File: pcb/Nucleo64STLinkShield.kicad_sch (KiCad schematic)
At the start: 0 parts

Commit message: Imported debug connector from design block.
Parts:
- added J1: Debug, pcb:Molex_PicoBlade_53047-1010_1x10_P1.25mm_Vertical, symbol Connector_Generic:Conn_02x05_Odd_Even
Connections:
- new net +3.3V: J1.1 (Pin_1)
- new net GND: J1.10 (Pin_10), J1.2 (Pin_2), J1.9 (Pin_9)
- new net RESET: J1.3 (Pin_3)
- new net STLINK_RX: J1.7 (Pin_7)
- new net STLINK_TX: J1.5 (Pin_5)
- new net SWCLK: J1.4 (Pin_4)
- new net SWDIO: J1.6 (Pin_6)
- new net SWO: J1.8 (Pin_8)
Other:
- note added: "Debug Connector."

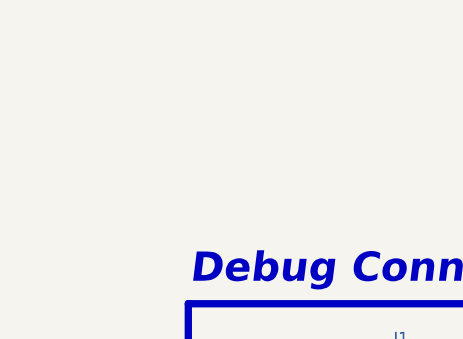
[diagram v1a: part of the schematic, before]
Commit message: Imported Nucleo-64 ST-Link debugger model.
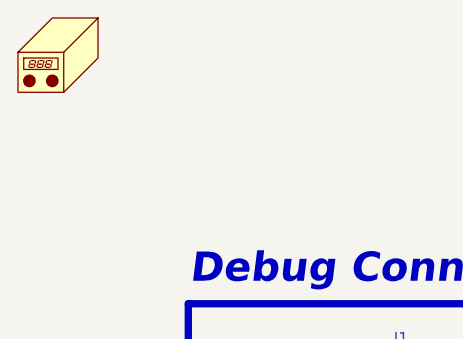
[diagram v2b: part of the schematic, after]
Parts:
- added N1: Housing, pcb:Nucleo64STLinkShieldHousing, symbol Mechanical:Housing
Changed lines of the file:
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@@
 		(dnp no)
 		(fields_autoplaced yes)
-		(property "Reference" "#PWR"
+		(property "Reference" "#PWR0101"
 			(at 142.24 100.33 0)
 			(effects
@@
 				(path "/0a179c33-cb18-4019-99e7-0e00d41f97d6/4084990c-2f2a-49e6-b0d0-e7eb5cede66f"
 					(reference "#PWR018")
+					(unit 1)
+				)
+			)
+			(project "Nucleo64STLinkShield"
+				(path "/dc931235-6a3d-461b-9fb0-f5879d72cf99"
+					(reference "#PWR0101")
+					(unit 1)
+				)
+			)
+		)
+	)
+	(symbol
+		(lib_id "Mechanical:Housing")
+		(at 107.95 62.23 0)
+		(unit 1)
+		(exclude_from_sim no)
+		(in_bom yes)
+		(on_board yes)
+		(dnp no)
+		(fields_autoplaced yes)
+		(property "Reference" "N1"
+			(at 111.76 61.2774 0)
+			(effects
+				(font
+					(size 1.27 1.27)
+				)
+				(justify left)
+				(hide yes)
+			)
+		)
+		(property "Value" "Housing"
+			(at 111.76 63.8174 0)
+			(effects
+				(font
+					(size 1.27 1.27)
+				)
+				(justify left)
+				(hide yes)
+			)
+		)
+		(property "Footprint" "pcb:Nucleo64STLinkShieldHousing"
+			(at 109.22 60.96 0)
+			(effects
+				(font
+					(size 1.27 1.27)
+				)
+				(hide yes)
+			)
+		)
+		(property "Datasheet" "~"
+			(at 109.22 60.96 0)
+			(effects
+				(font
+					(size 1.27 1.27)
+				)
+				(hide yes)
+			)
+		)
+		(property "Description" "Housing"
+			(at 107.95 62.23 0)
+			(effects
+				(font
+					(size 1.27 1.27)
+				)
+				(hide yes)
+			)
+		)
+		(instances
+			(project ""
+				(path "/dc931235-6a3d-461b-9fb0-f5879d72cf99"
+					(reference "N1")
 					(unit 1)
 				)
@@
 		(dnp no)
 		(fields_autoplaced yes)
-		(property "Reference" "#PWR"
+		(property "Reference" "#PWR0103"
 			(at 157.48 110.49 0)
 			(effects
@@
 				(path "/0a179c33-cb18-4019-99e7-0e00d41f97d6/4084990c-2f2a-49e6-b0d0-e7eb5cede66f"
 					(reference "#PWR017")
+					(unit 1)
+				)
+			)
+			(project "Nucleo64STLinkShield"
+				(path "/dc931235-6a3d-461b-9fb0-f5879d72cf99"
+					(reference "#PWR0103")
 					(unit 1)
 				)
@@
 		(dnp no)
 		(fields_autoplaced yes)
-		(property "Reference" "#PWR"
+		(property "Reference" "#PWR0102"
 			(at 132.08 110.49 0)
 			(effects
@@
 				(path "/0a179c33-cb18-4019-99e7-0e00d41f97d6/4084990c-2f2a-49e6-b0d0-e7eb5cede66f"
 					(reference "#PWR019")
+					(unit 1)
+				)
+			)
+			(project "Nucleo64STLinkShield"
+				(path "/dc931235-6a3d-461b-9fb0-f5879d72cf99"
+					(reference "#PWR0102")
 					(unit 1)
 				)
@@
 		(dnp no)
 		(fields_autoplaced yes)
-		(property "Reference" "#PWR"
+		(property "Reference" "#PWR0104"
 			(at 157.48 100.33 0)
 			(effects
@@
 					(unit 1)
 				)
+			)
+			(project "Nucleo64STLinkShield"
+				(path "/dc931235-6a3d-461b-9fb0-f5879d72cf99"
+					(reference "#PWR0104")
+					(unit 1)
+				)

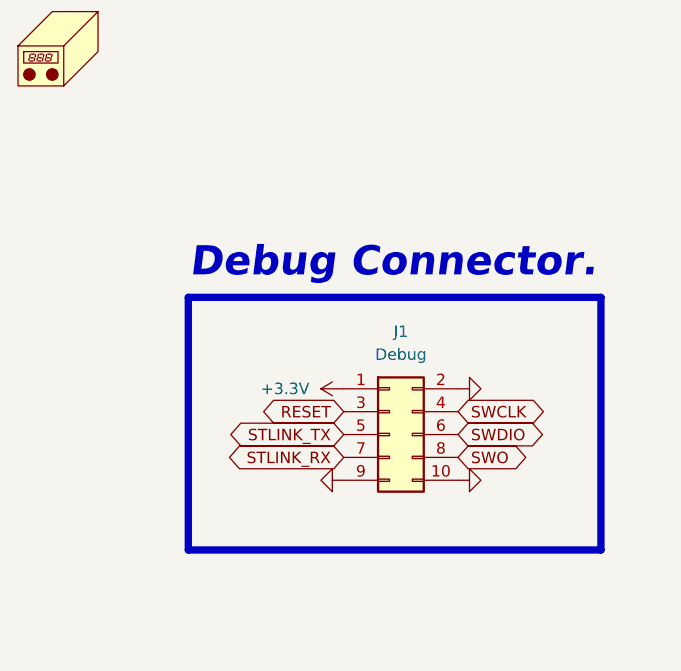
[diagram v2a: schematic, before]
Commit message: Updated debug connector symbol from 02x05 to 01x10.
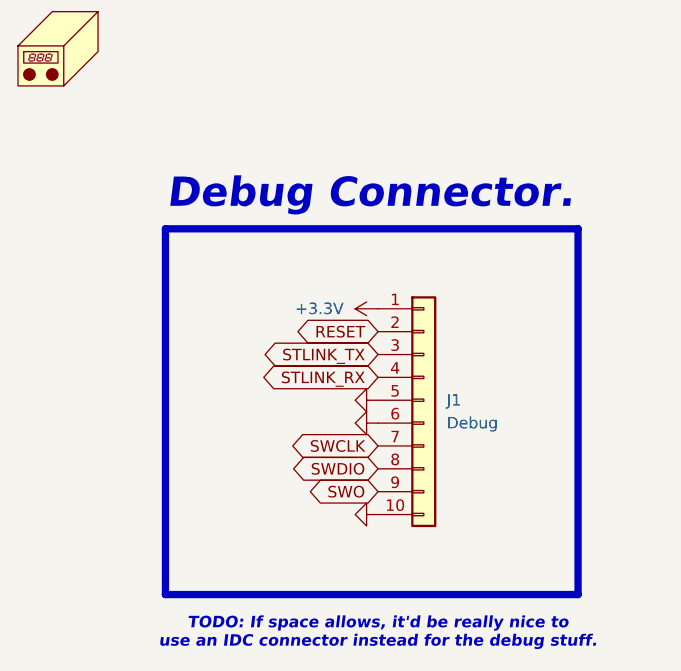
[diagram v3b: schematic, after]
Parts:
- removed J1: Debug, pcb:Molex_PicoBlade_53047-1010_1x10_P1.25mm_Vertical, symbol Connector_Generic:Conn_02x05_Odd_Even
- added J1: Debug, pcb:Molex_PicoBlade_53047-1010_1x10_P1.25mm_Vertical, symbol Connector_Generic:Conn_01x10
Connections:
- net +3.3V: now also J1.1 (Pin_1)
- net GND: now also J1.10 (Pin_10), J1.5 (Pin_5), J1.6 (Pin_6)
- net RESET: now also J1.2 (Pin_2)
- net STLINK_RX: now also J1.4 (Pin_4)
- net STLINK_TX: now also J1.3 (Pin_3)
- net SWCLK: now also J1.7 (Pin_7)
- net SWDIO: now also J1.8 (Pin_8)
- net SWO: now also J1.9 (Pin_9)
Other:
- note added: "TODO: If space allows, it'd be really nice to use an IDC connector instead for the debug stuff."

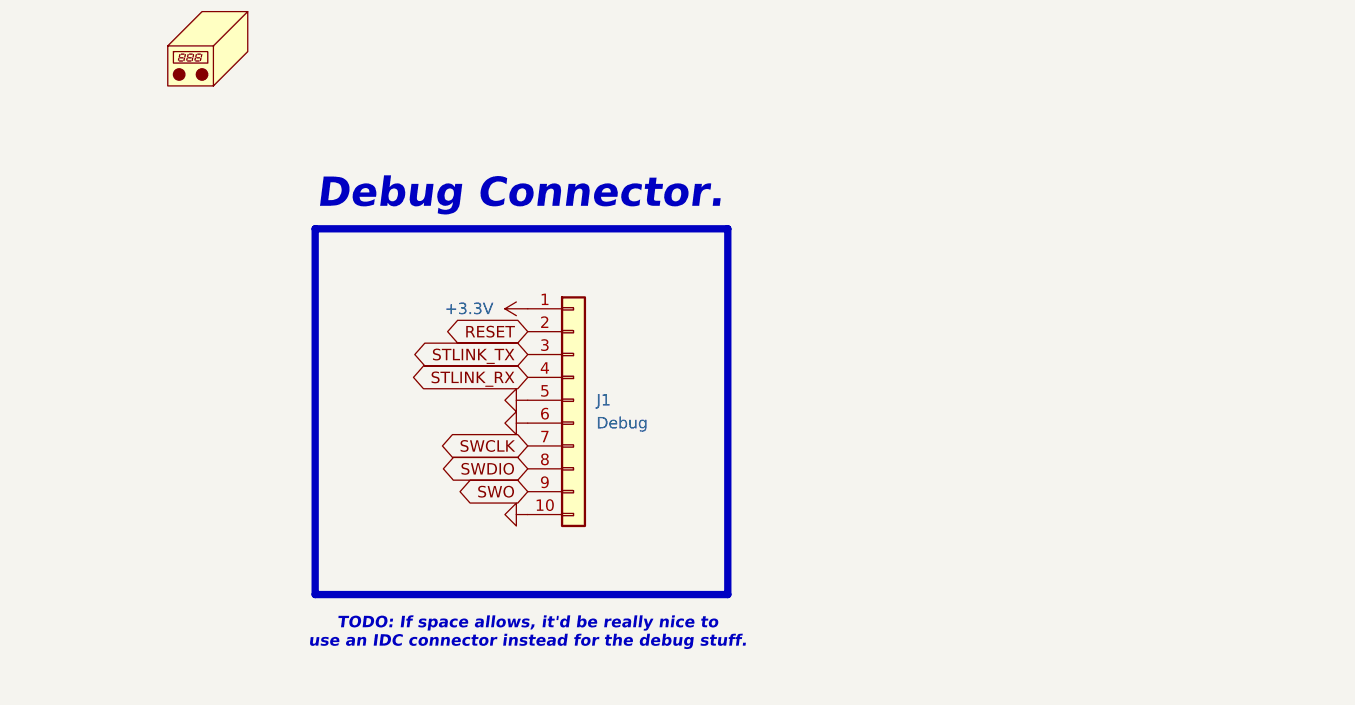
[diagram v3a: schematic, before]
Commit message: Made edge cuts.
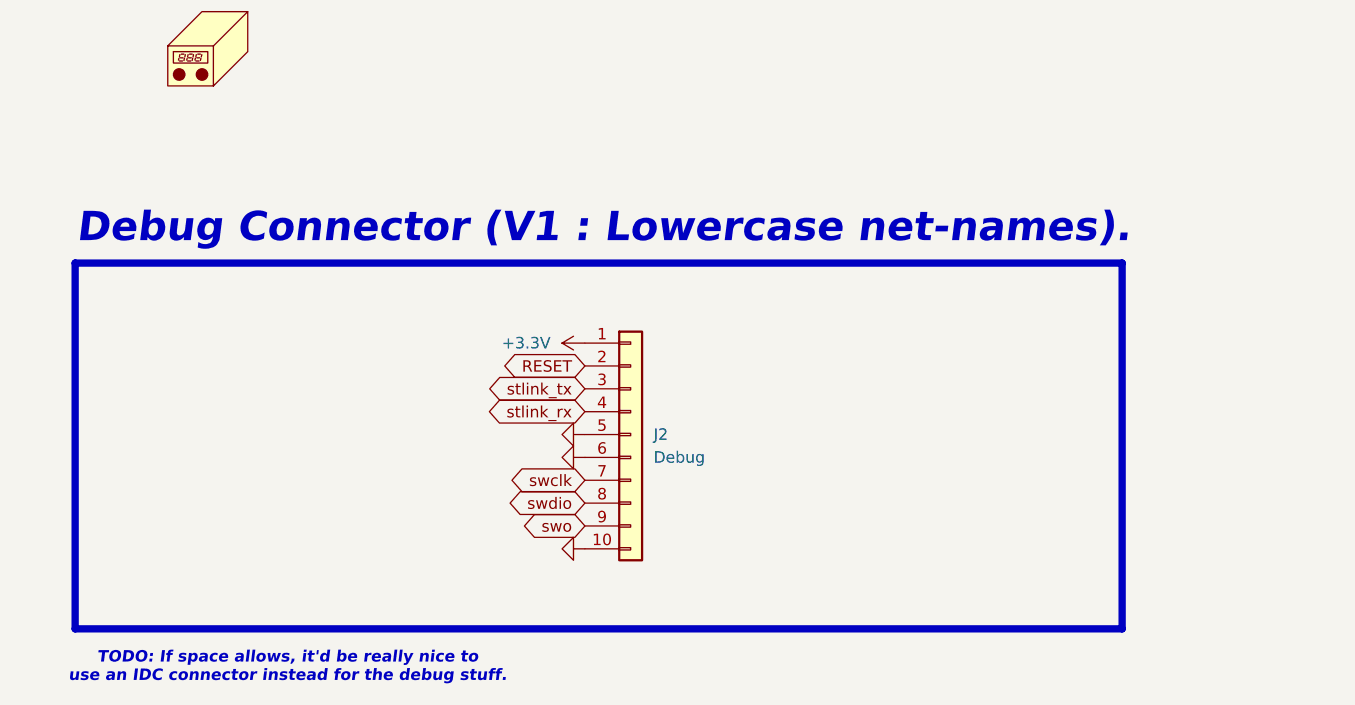
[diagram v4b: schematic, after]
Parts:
- removed J1: Debug, pcb:Molex_PicoBlade_53047-1010_1x10_P1.25mm_Vertical, symbol Connector_Generic:Conn_01x10
- added J2: Debug, pcb:Molex_PicoBlade_53047-1010_1x10_P1.25mm_Vertical, symbol Connector_Generic:Conn_01x10
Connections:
- net +3.3V: now also J2.1 (Pin_1)
- net GND: now also J2.10 (Pin_10), J2.5 (Pin_5), J2.6 (Pin_6)
- net RESET: now also J2.2 (Pin_2)
- new net stlink_rx: J2.4 (Pin_4)
- new net stlink_tx: J2.3 (Pin_3)
- new net swclk: J2.7 (Pin_7)
- new net swdio: J2.8 (Pin_8)
- new net swo: J2.9 (Pin_9)
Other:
- note added: "Debug Connector (V1 : Lowercase net-names)."
- note removed: "Debug Connector."

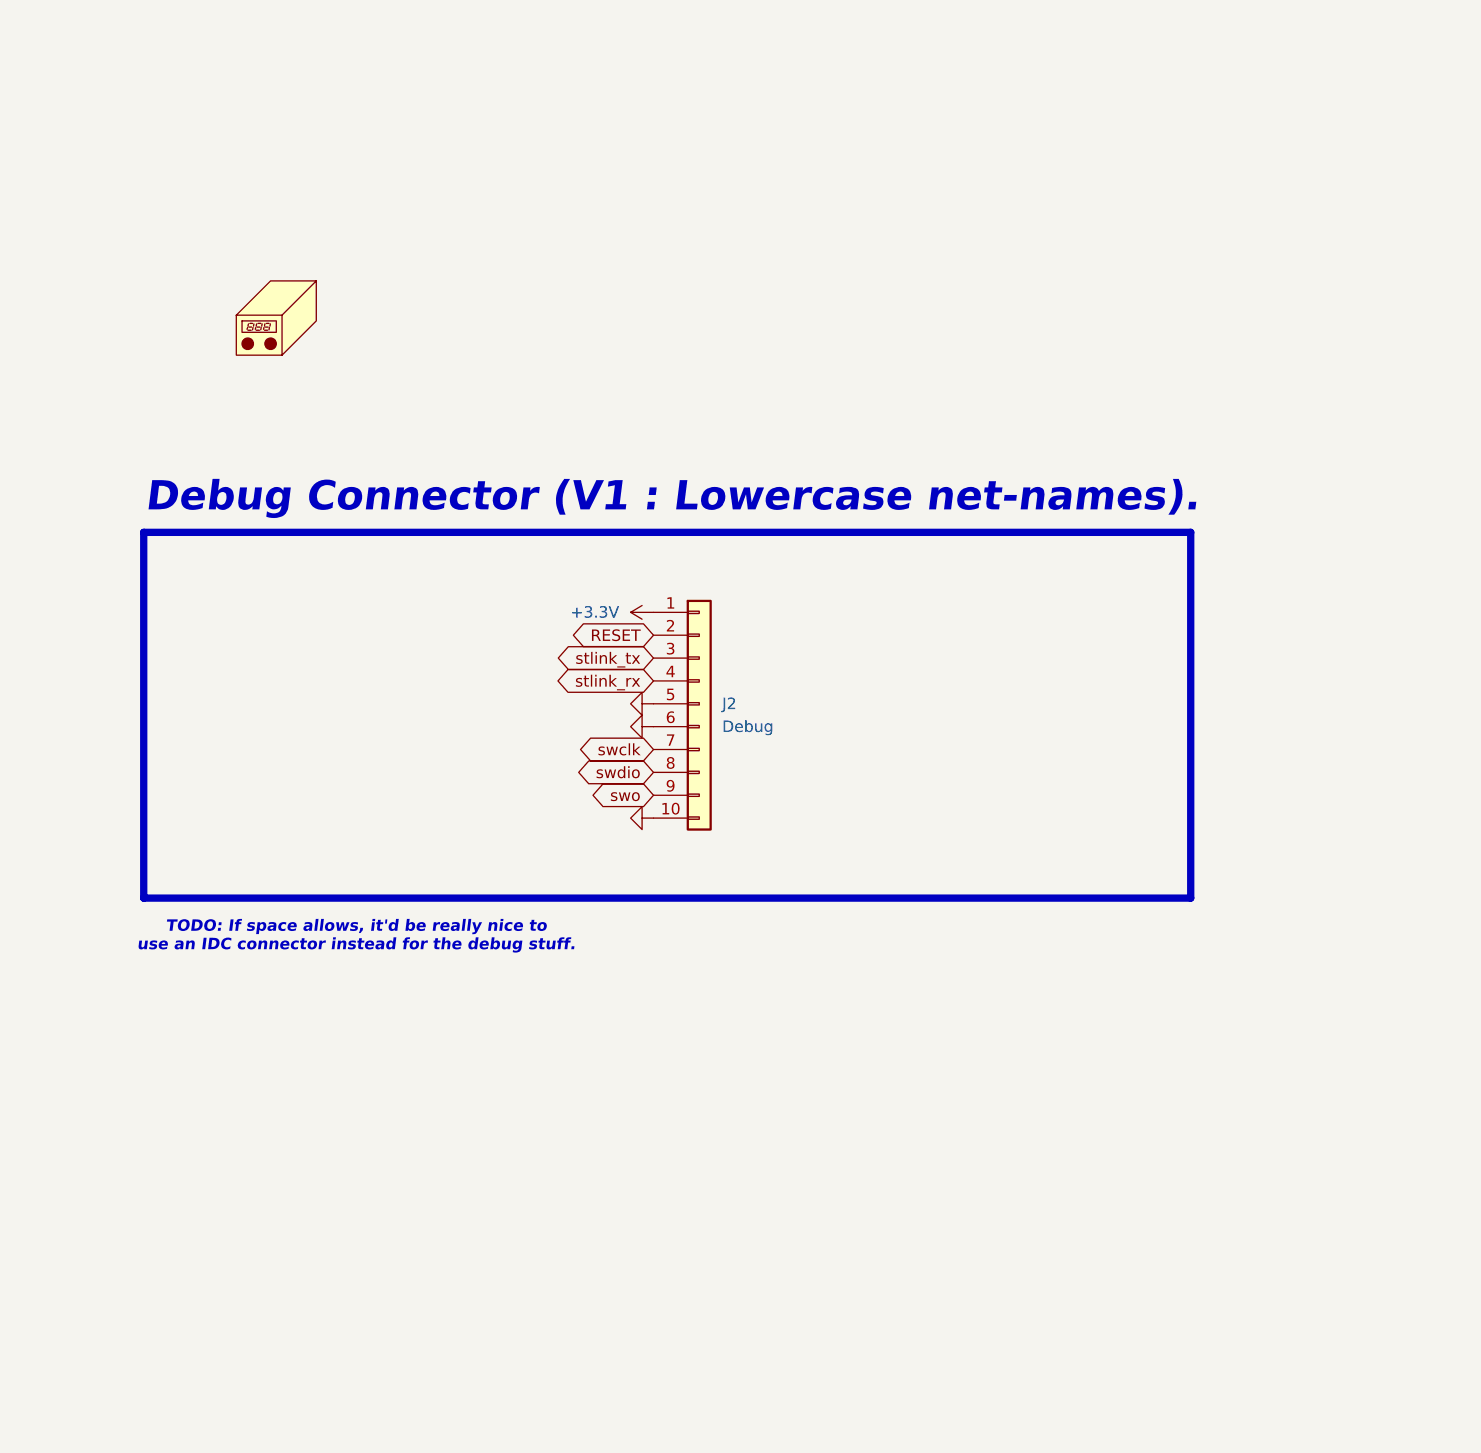
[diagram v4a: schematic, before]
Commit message: Added 2.54mm pin sockets to ST-Link.
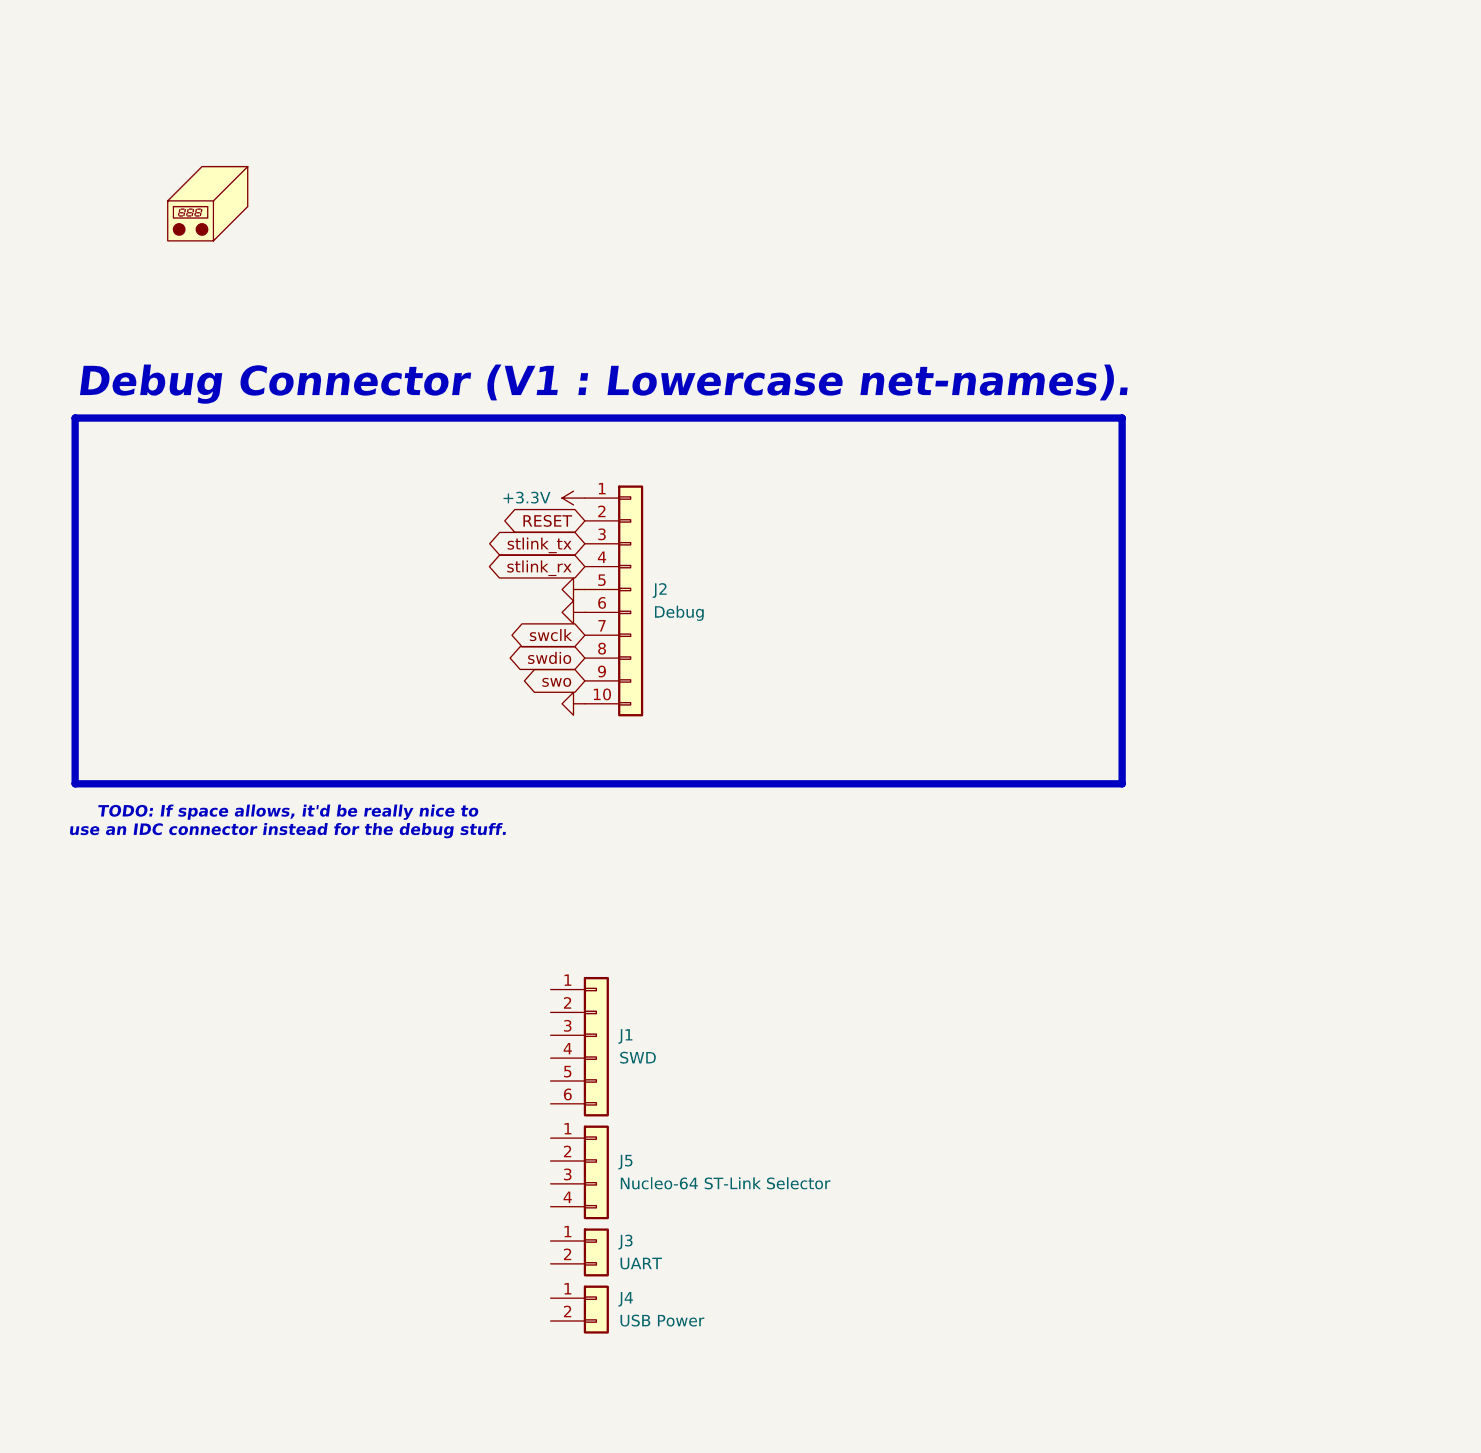
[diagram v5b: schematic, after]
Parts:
- added J1: SWD, Connector_PinSocket_2.54mm:PinSocket_1x06_P2.54mm_Vertical, symbol Connector_Generic:Conn_01x06
- added J3: UART, Connector_PinSocket_2.54mm:PinSocket_1x02_P2.54mm_Vertical, symbol Connector_Generic:Conn_01x02
- added J4: USB Power, Connector_PinSocket_2.54mm:PinSocket_1x02_P2.54mm_Vertical, symbol Connector_Generic:Conn_01x02
- added J5: Nucleo-64 ST-Link Selector, Connector_PinSocket_2.54mm:PinSocket_1x04_P2.54mm_Vertical, symbol Connector_Generic:Conn_01x04
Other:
- moved on the sheet: J2
